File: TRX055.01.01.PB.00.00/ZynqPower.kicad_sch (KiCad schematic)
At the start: 87 parts, among them U1 XC7Z015-1CLG485I, U5 AP22913CN4, U7 TCR2LN10,LF, U8 TCR2LN12,LF, U9 AP22913CN4

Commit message: Update Layout
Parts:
- removed FB1, FB2, FB3, FB4, FB5: FerriteBead, Inductor_SMD:L_0603_1608Metric, symbol Device:FerriteBead
- C26, C28, C29, C30, C31, C32, C33, C34, C35, C36, C37, C38, C39, C40, C41, C42, C43, C44, C45, C46, C47, C48, C49, C50, C51, C52, C53, C54, C55, C56, C57, C58, C59, C60, C61, C62, C63, C64, C65, C66, C67, C68, C69, C70, C71, C72, C73, C74, C75, C76, C77, C78, C79, C80, C81, C82, C83, C84, C85, C86, C87: Material X5R -> X7R; Voltage 10V -> 100V
- U1: footprint XC7Z015:CLG485XC7Z012S&slash_XC7Z015_AMD -> CLG485XC7Z012S/XC7Z015_AMD; JLCPCB Part # (none) -> C1522056
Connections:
- net PS_CORE is gone; now on net 1V_RAIL_A: C51.1, C52.1, C53.1, C54.1, C55.1, C56.1, U1.G15 (VCCPINT), U1.H14 (VCCPINT), U1.J15 (VCCPINT), U1.L15 (VCCPINT), U1.N15 (VCCPINT), U1.R15 (VCCPINT)
- net VCCAUX is gone; now on net VCC_MIO: C36.1, C37.1, C38.1, C39.1, U1.N13 (VCCAUX), U1.P12 (VCCAUX), U1.R13 (VCCAUX), U1.T12 (VCCAUX)
- net VCCBRAM is gone; now on net 1V_RAIL_B: U1.H12 (VCCBRAM), U1.J13 (VCCBRAM)
- net VCCINT is gone; now on net 1V_RAIL_B: C28.1, C29.1, C30.1, C31.1, C32.1, C33.1, C34.1, C35.1, U1.J11 (VCCINT), U1.J9 (VCCINT), U1.K10 (VCCINT), U1.L9 (VCCINT), U1.M10 (VCCINT), U1.N9 (VCCINT), U1.P10 (VCCINT), U1.R9 (VCCINT)
- net VCCPAUX is gone; now on net 1V8_RAIL_A: C57.1, C58.1, C59.1, C60.1, U1.K14 (VCCPAUX), U1.L13 (VCCPAUX), U1.M14 (VCCPAUX), U1.P14 (VCCPAUX)
- net VCC_MIO: now reaches FB11.1, U5.A1 (OUT)
- net VCC_MIO: now also U1.A13 (VCCO_MIO1_501), U1.B10 (VCCO_MIO1_501), U1.B20 (VCCO_MIO0_500), U1.C17 (VCCO_MIO0_500), U1.D14 (VCCO_MIO1_501), U1.E11 (VCCO_MIO1_501)

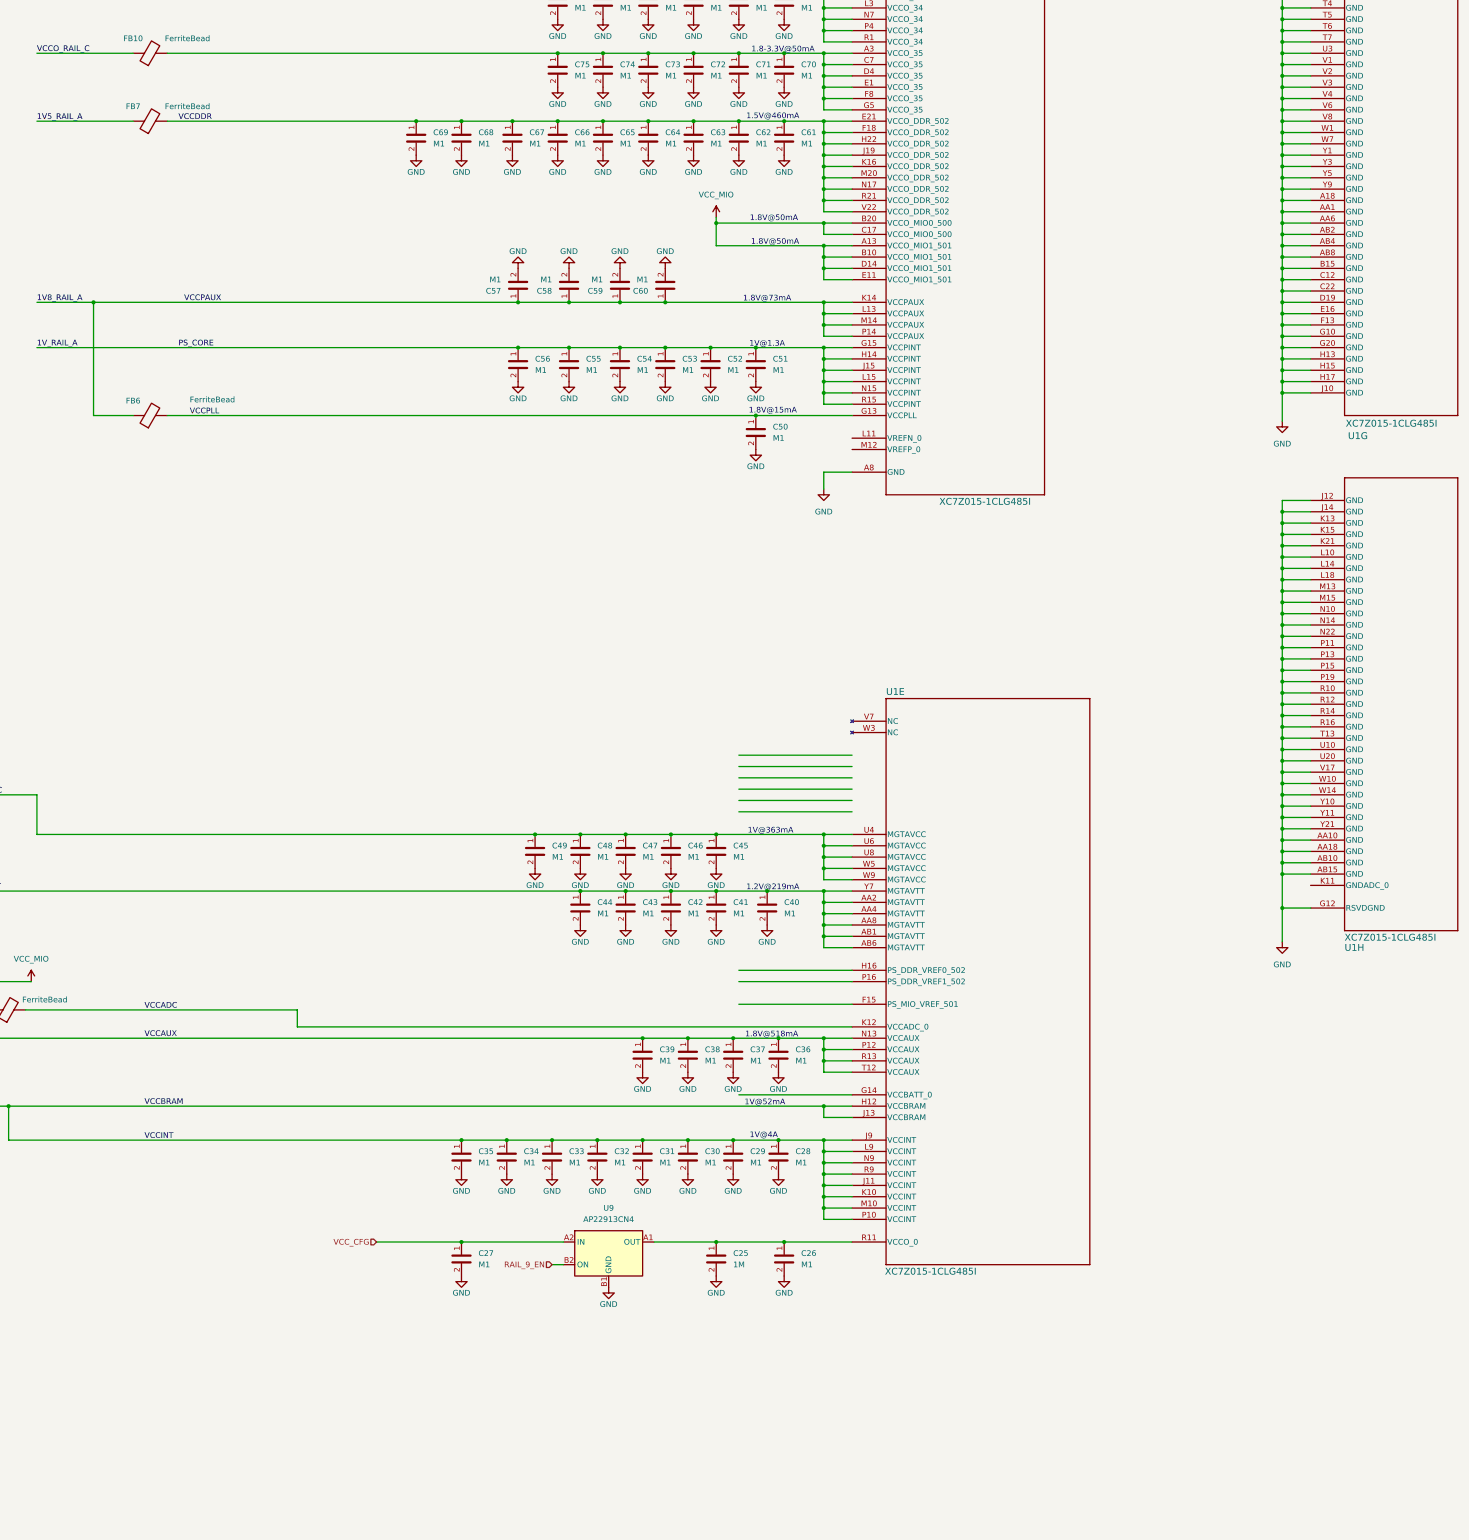
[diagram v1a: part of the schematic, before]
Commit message: +ETH +USB +Connectors
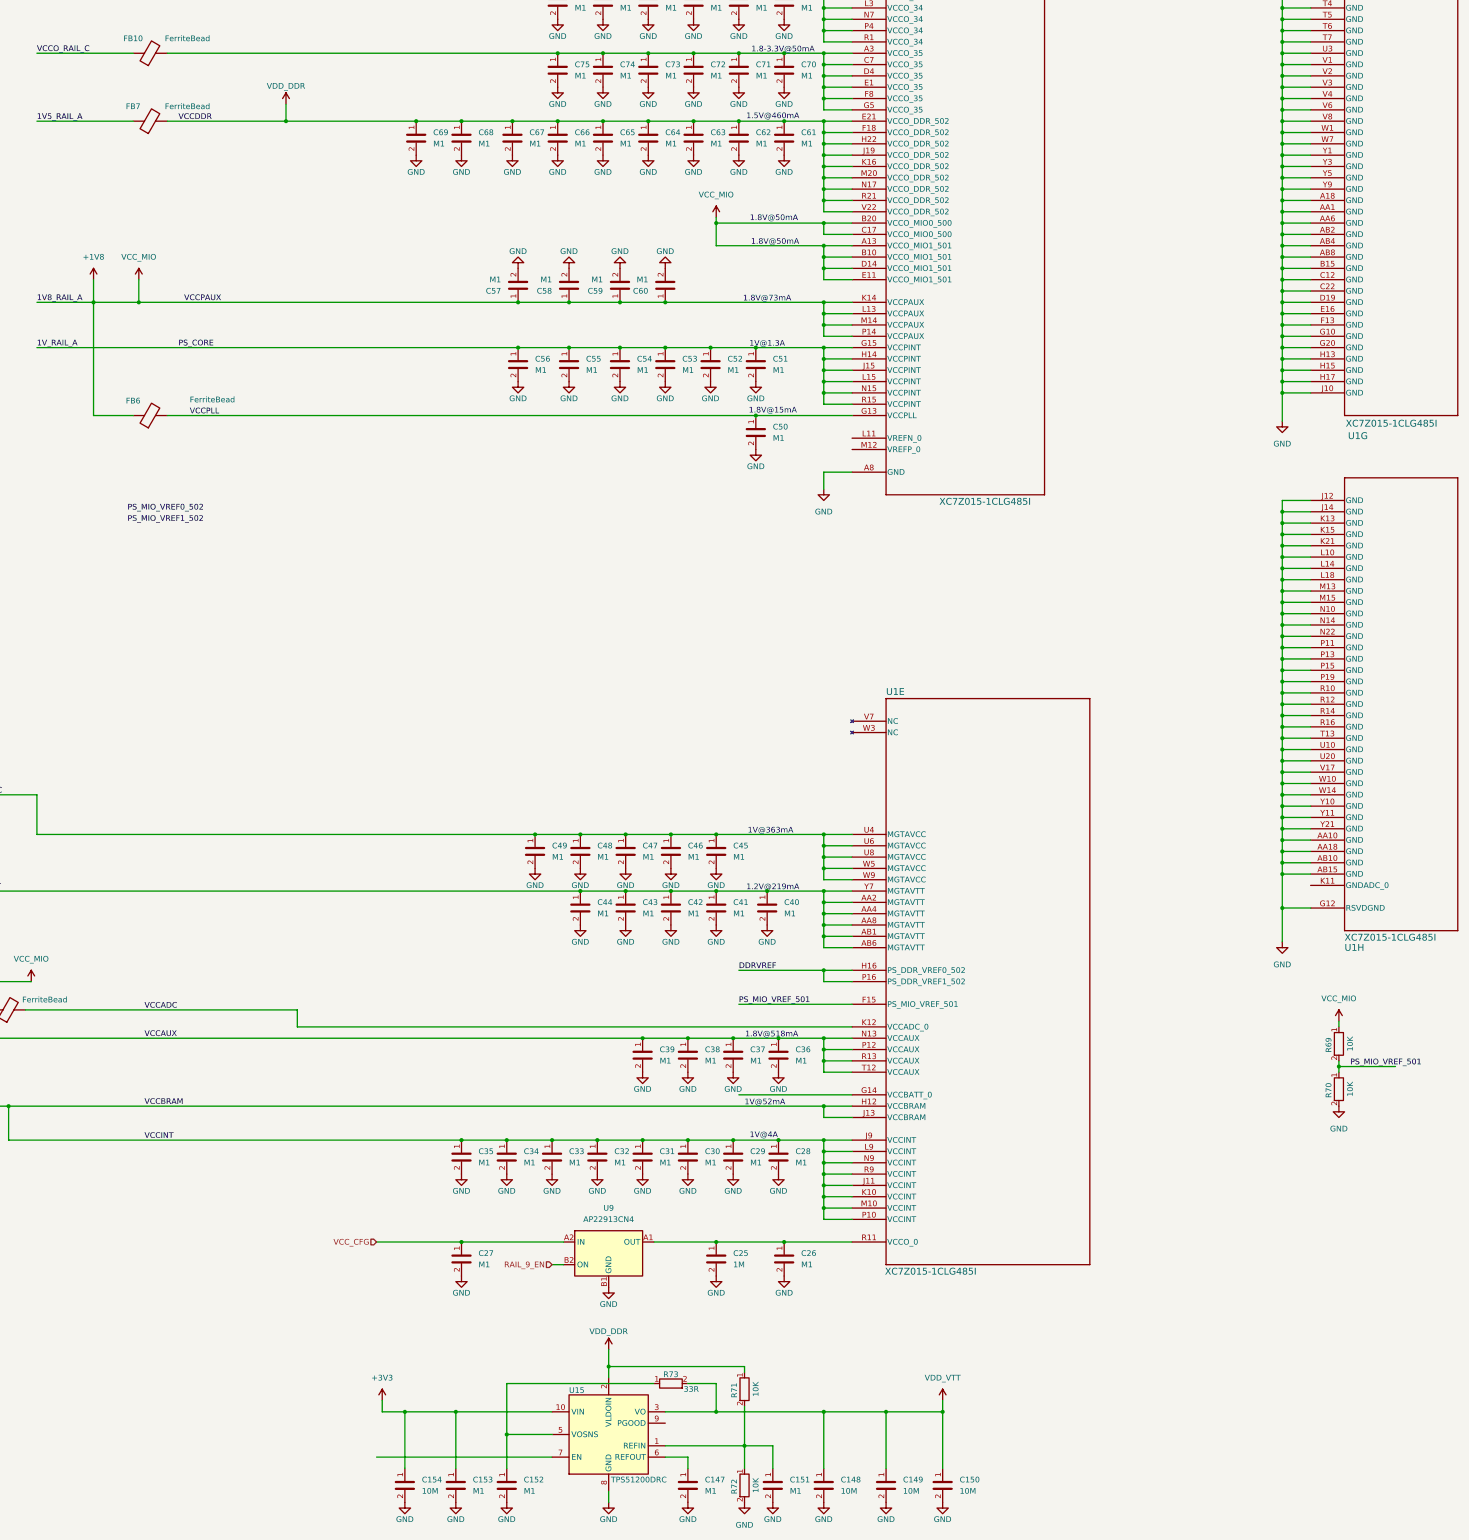
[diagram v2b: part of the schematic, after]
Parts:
- added C147, C151, C152, C153: M1, Capacitor_SMD:C_0402_1005Metric, symbol PPA-Pasive:Cap
- added C148, C149, C150, C154: 10M, Capacitor_SMD:C_0603_1608Metric, symbol PPA-Pasive:Cap
- added R69, R70, R71, R72: 10K, Resistor_SMD:R_0402_1005Metric, symbol PPA-Pasive:Res
- added R73: 33R, Resistor_SMD:R_0402_1005Metric, symbol PPA-Pasive:Res
- added U15: TPS51200DRC, Package_SON:VSON-10-1EP_3x3mm_P0.5mm_EP1.65x2.4mm, symbol Regulator_Linear:TPS51200DRC
- C26, C27, C28, C29, C30, C31, C32, C33, C34, C35, C36, C37, C38, C39, C40, C41, C42, C43, C44, C45, C46, C47, C48, C49, C50, C51, C52, C53, C54, C55, C56, C57, C58, C59, C60, C61, C62, C63, C64, C65, C66, C67, C68, C69, C70, C71, C72, C73, C74, C75, C76, C77, C78, C79, C80, C81, C82, C83, C84, C85, C86, C87: footprint Capacitor_SMD:C_0201_0603Metric -> Capacitor_SMD:C_0402_1005Metric
- FB10, FB11, FB6, FB7, FB8, FB9: footprint Inductor_SMD:L_0603_1608Metric -> Resistor_SMD:R_01005_0402Metric
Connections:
- net VCC_MIO is gone; now on net +1V8: C36.1, C37.1, C38.1, C39.1, FB11.1, U1.A13 (VCCO_MIO1_501), U1.B10 (VCCO_MIO1_501), U1.B20 (VCCO_MIO0_500), U1.C17 (VCCO_MIO0_500), U1.D14 (VCCO_MIO1_501), U1.E11 (VCCO_MIO1_501), U1.N13 (VCCAUX), U1.P12 (VCCAUX), U1.R13 (VCCAUX), U1.T12 (VCCAUX), U5.A1 (OUT)
- net GND: now also C147.2, C148.2, C149.2, C150.2, C151.2, C152.2, C153.2, C154.2, R70.2, R72.2, U15.11 (GND), U15.4 (GND), U15.8 (GND)
- net PS_MIO_VREF_501: now reaches U1.F15 (PS_MIO_VREF_501)
- net PS_MIO_VREF_501: now also R69.2, R70.1
- net DDRVREF: now reaches U1.H16 (PS_DDR_VREF0_502)
- net DDRVREF: now also U1.P16 (PS_DDR_VREF1_502)
- net 1V8_RAIL_A renamed +1V8
- net +1V8: now also R69.1
- net VCCDDR renamed VDD_DDR
- net VDD_DDR: now also R71.1, U15.2 (VLDOIN)
- new net: C151.1, R71.2, R72.1, U15.1 (REFIN)
- new net: C152.1, R73.1, U15.5 (VOSNS)
- new net: C147.1, U15.6 (REFOUT)
- new net +3V3: C153.1, C154.1, U15.10 (VIN)
- new net VDD_VTT: C148.1, C149.1, C150.1, R73.2, U15.3 (VO)

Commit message: + add clocks + add PSU
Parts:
- removed U5, U9: AP22913CN4, Package_CSP:WLCSP-4-X1-WLB0909-4_0.89x0.89mm_P0.5mm, symbol Power_Management:AP22913CN4
- removed U7: TCR2LN10,LF, FOOT-PPA-CONN:SDFN4E, symbol ppa-ic-power:TCR2LN
- removed U8: TCR2LN12,LF, FOOT-PPA-CONN:SDFN4E, symbol ppa-ic-power:TCR2LN
- added C184, C185: M1, Capacitor_SMD:C_0201_0603Metric, symbol PPA-Pasive:Cap
- added C240, C244: 1M, Capacitor_SMD:C_0402_1005Metric, symbol PPA-Pasive:Cap
- added C245, C246, C247, C248: 10M, Capacitor_SMD:C_0603_1608Metric, symbol PPA-Pasive:Cap
- added FB37, FB38: BLM18PG330SN1D, Inductor_SMD:L_0603_1608Metric, symbol Device:FerriteBead
- added JP1, JP2, JP3, JP4, JP5, JP6, JP7, JP8: Jumper_2_Open, foot-ppa-passive:SolderJumper-2_P1.3mm_open_Pad1.0x1.5mm, symbol Jumper:Jumper_2_Open
- added R5, R6, R7, R8: 10K, Resistor_SMD:R_0402_1005Metric, symbol PPA-Pasive:Res
- added U24: SIP32409DNP-T1-GE4, ppa-active:UDFN-5_L1.6-W1.2-P0.50-BL-EP, symbol ppa-ic-power:SIP32409DNP-T1-GE4
- added U5, U8: NCP186AMN080TBG, ppa-active:DFN-12_L4.0-W4.0-P0.65-BL-EP3.4, symbol ppa-ic-power:NCP186AMN080TBG
- C10, C11, C12, C13, C14, C148, C149, C15, C150, C154, C16, C9: JLCPCB Part # (none) -> C96446
- C147, C151, C152, C153, C26, C27, C28, C29, C30, C31, C32, C33, C34, C35, C36, C37, C38, C39, C40, C41, C42, C43, C44, C45, C46, C47, C48, C49, C50, C51, C52, C53, C54, C55, C56, C57, C58, C59, C60, C61, C62, C63, C64, C65, C66, C67, C68, C69, C70, C71, C72, C73, C74, C75, C76, C77, C78, C79, C80, C81, C82, C83, C84, C85, C86, C87: footprint Capacitor_SMD:C_0402_1005Metric -> Capacitor_SMD:C_0201_0603Metric; JLCPCB Part # (none) -> C1581
- C25: JLCPCB Part # (none) -> C52923
- FB10, FB7, FB8, FB9: value FerriteBead -> BLM18PG330SN1D; footprint Resistor_SMD:R_01005_0402Metric -> Inductor_SMD:L_0603_1608Metric; JLCPCB Part # (none) -> C88984
- FB11, FB6: value FerriteBead -> GZ1005U102TF; footprint Resistor_SMD:R_01005_0402Metric -> Inductor_SMD:L_0402_1005Metric_Pad0.77x0.64mm_HandSolder; JLCPCB Part # (none) -> C19136
- R69, R70, R71, R72: JLCPCB Part # (none) -> C25744
- R73: JLCPCB Part # (none) -> C25105
- U1: value XC7Z015-1CLG485I -> XC7Z015-2CLG485I; JLCPCB Part # C1522056 -> C1522056
- U15: JLCPCB Part # (none) -> C34771
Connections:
- net VCC_CFG is gone; now on net +1V8: C27.1
- net +1V8: now also C25.1, C26.1, U1.R11 (VCCO_0), JP4.2 (B), U24.1 (IN); no longer C12.1, C36.1, C37.1, C38.1, C39.1, FB11.1, U1.N13 (VCCAUX), U1.P12 (VCCAUX), U1.R13 (VCCAUX), U1.T12 (VCCAUX)
- net +3V3: now also JP7.2 (B)
- net 1V5_RAIL_A: now also C247.1, C248.1, JP8.2 (B), U5.10 (IN), U5.11 (IN), U8.10 (IN), U8.11 (IN); no longer C14.1
- net 1V_RAIL_A: now also JP2.2 (B); no longer C9.1
- net 1V_RAIL_B: now also JP3.2 (B); no longer C11.1
- net GND: now also U1.K11 (GNDADC_0), C184.2, C185.2, C240.2, C244.2, C245.2, C246.2, C247.2, C248.2, R6.2, R8.2, U24.2 (GND), U24.5 (EXP), U5.13 (EP), U5.8 (GND), U8.13 (EP), U8.8 (GND)
- net MGTAVCC: now also C245.1, FB38.2
- net MGTAVTT: now also C246.1, FB37.2
- net RAIL_7_EN: now also U5.9 (EN), U8.9 (EN)
- net RAIL_8_EN: now also U24.3 (EN)
- net VCCADC: now also C184.1, C185.1
- net VCCO_RAIL_A: now also FB9.1, JP5.2 (B); no longer C10.1, FB8.1
- net VCCO_RAIL_B: now also FB8.1, JP6.2 (B); no longer C13.1, FB9.1
- net VCCO_RAIL_C: now also JP1.2 (B); no longer C16.1
- net VCCIO_35: now reaches C70.1, C71.1, C72.1, C73.1, C74.1, C75.1, FB10.2, U1.A3 (VCCO_35), U1.C7 (VCCO_35), U1.D4 (VCCO_35), U1.E1 (VCCO_35), U1.F8 (VCCO_35), U1.G5 (VCCO_35)
- net VCCIO_13: now reaches C82.1, C83.1, C84.1, C85.1, C86.1, C87.1, U1.AA13 (VCCO_13), U1.AB20 (VCCO_13), U1.T18 (VCCO_13), U1.U15 (VCCO_13), U1.V12 (VCCO_13), U1.W19 (VCCO_13), U1.Y16 (VCCO_13)
- net VCCIO_13: now also FB9.2; no longer FB8.2
- net VCCIO_34: now reaches C76.1, C77.1, C78.1, C79.1, C80.1, C81.1, U1.H2 (VCCO_34), U1.K6 (VCCO_34), U1.L3 (VCCO_34), U1.N7 (VCCO_34), U1.P4 (VCCO_34), U1.R1 (VCCO_34)
- net VCCIO_34: now also FB8.2; no longer FB9.2
- net 3V3_RAIL_MAIN renamed QBUCK_LP87524J1/BUCK2
- net QBUCK_LP87524J1/BUCK2: now also JP7.1 (A)
- new net: R5.2, R6.1, U8.5 (FB/ADJ)
- new net: C240.1, FB38.1, R7.1, U5.2 (OUT), U5.3 (OUT)
- new net: C244.1, FB37.1, R5.1, U8.2 (OUT), U8.3 (OUT)
- new net: U5.1 (N/C), U5.4 (N/C)
- new net: U5.12 (N/C), U5.6 (N/C)
- new net: R7.2, R8.1, U5.5 (FB/ADJ)
- new net: U8.1 (N/C), U8.4 (N/C)
- new net: U8.12 (N/C), U8.6 (N/C)
- new net QBUCK_LP87524J/BUCK0: C10.1, JP1.1 (A)
- new net QBUCK_LP87524J/BUCK1: C9.1, JP2.1 (A)
- new net QBUCK_LP87524J/BUCK2: C11.1, JP3.1 (A)
- new net QBUCK_LP87524J/BUCK3: C12.1, JP4.1 (A)
- new net QBUCK_LP87524J1/BUCK0: C13.1, JP5.1 (A)
- new net QBUCK_LP87524J1/BUCK1: C14.1, JP6.1 (A)
- new net QBUCK_LP87524J1/BUCK3: C16.1, JP8.1 (A)
- new net VCCAUX: C36.1, C37.1, C38.1, C39.1, FB11.1, U1.N13 (VCCAUX), U1.P12 (VCCAUX), U1.R13 (VCCAUX), U1.T12 (VCCAUX), U24.4 (OUT)
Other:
- note added: "1"
- note added: "2"
- note added: "3"
- note added: "4"
- note added: "5"
- note added: "6"
- note added: "7"
- note added: "8"
- moved on the sheet: C147, C148, C149, C150, C151, C152, C153, C154, C25, C26, C27, C28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

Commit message: V0.1 - production, added brig-up comments
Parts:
- added R162: 5K1, Resistor_SMD:R_0402_1005Metric, symbol PPA-Pasive:Res
- R5, R7: value 10K -> 5K1; JLCPCB Part # C25744 -> C25905
- U1: footprint CLG485XC7Z012S/XC7Z015_AMD -> XC7Z015:CLG485XC7Z012S&slash_XC7Z015_AMD
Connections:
- net +1V8: now also C247.1, C248.1, U5.10 (IN), U5.11 (IN), U8.10 (IN), U8.11 (IN); no longer C25.1, C26.1, C27.1, U1.R11 (VCCO_0)
- net 1V5_RAIL_A: no longer C247.1, C248.1, U5.10 (IN), U5.11 (IN), U8.10 (IN), U8.11 (IN)
- net GND: now also U1.L11 (VREFN_0), U1.M12 (VREFP_0)
- net RAIL_7_EN: no longer U8.9 (EN)
- net RAIL_9_EN: now also U15.7 (EN)
- net at C240.1, FB38.1, R7.1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: now also R162.1
- net VREF_DDR: now reaches C147.1, U15.6 (REFOUT)
- net +1V2: now reaches C244.1, FB37.1, R5.1, U8.2 (OUT), U8.3 (OUT)
- net at U5.1 (N/C): no longer U5.4 (N/C)
- net at U5.12 (N/C): no longer U5.6 (N/C)
- net at R7.2, R8.1, U5.5 (FB/ADJ): now also R162.2
- net at U8.1 (N/C): no longer U8.4 (N/C)
- net at U8.12 (N/C): no longer U8.6 (N/C)
- net 1V_RAIL_A renamed VDD_1V_RAIL_A
- net 1V_RAIL_B renamed VDD_1V_RAIL_B
- net QBUCK_LP87524J/BUCK0 renamed SR_A0
- net QBUCK_LP87524J/BUCK1 renamed SR_A1
- net QBUCK_LP87524J/BUCK2 renamed SR_A2
- net QBUCK_LP87524J/BUCK3 renamed SR_A3
- net QBUCK_LP87524J1/BUCK0 renamed SR_B0
- net QBUCK_LP87524J1/BUCK1 renamed SR_B1
- net QBUCK_LP87524J1/BUCK2 renamed SR_B2
- net QBUCK_LP87524J1/BUCK3 renamed SR_B3
- new net RAIL_10_EN: U8.9 (EN)
- new net VCC_CFG: C25.1, C26.1, C27.1, U1.R11 (VCCO_0)
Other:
- note removed: "TPS51397A"
- company: (none) -> Tronex s.r.o. / Tronex Group USA LLC
- title: (none) -> TRNX SDR Carrier board
- moved on the sheet: C247, C248, C27, R5, R6, R69, R70, R8, U5, U8
